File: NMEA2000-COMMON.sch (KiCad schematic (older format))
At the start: 65 parts, among them J2 CAN, SW1 PRG, SW2 INSTANCE, SW3 BUS, U1 MCP2551-I-P, U101 74LS165, U2 TMR-2-2411, U3 74HCT595, U4 74HCT595, U5 Teensy_4.0

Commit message: Tweak
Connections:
- net TRANSMIT_LED: no longer names the net of D5.2 (A), U5.17 (D15)
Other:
- moved on the sheet: C1, C3, C5, D5, F1, J2, R1, R2, R3, R36, R37, R38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

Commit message: Reroute
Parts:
- U101: value 74LS165 -> 74HC165
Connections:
- net GND: now also U101.10 (DS), U101.15 (~CE)
- net INSTANCE_CE renamed D9
- net D9: no longer U101.15 (~CE)
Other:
- note added: "CONFIGURATION"
- note removed: "Opto-isolated SPST inputs. Each opto-isolator\nis driven by a constant current source which\noperates the isolator LED at 6mA from voltages\nin the range 5VDC through 50VDC."
- moved on the sheet: C1, C101, C5, F1, J2, R1, R101, R102, R103, R104, R105, R106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

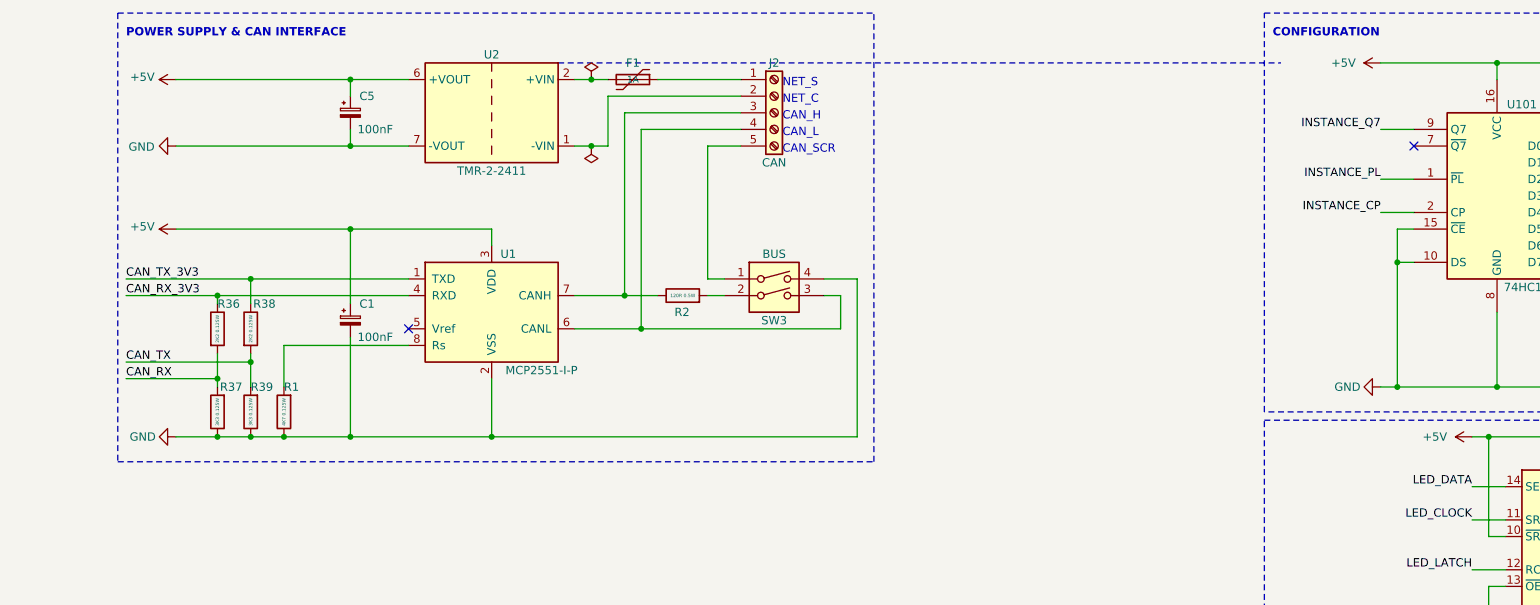
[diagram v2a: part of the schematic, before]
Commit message: Add level shifters
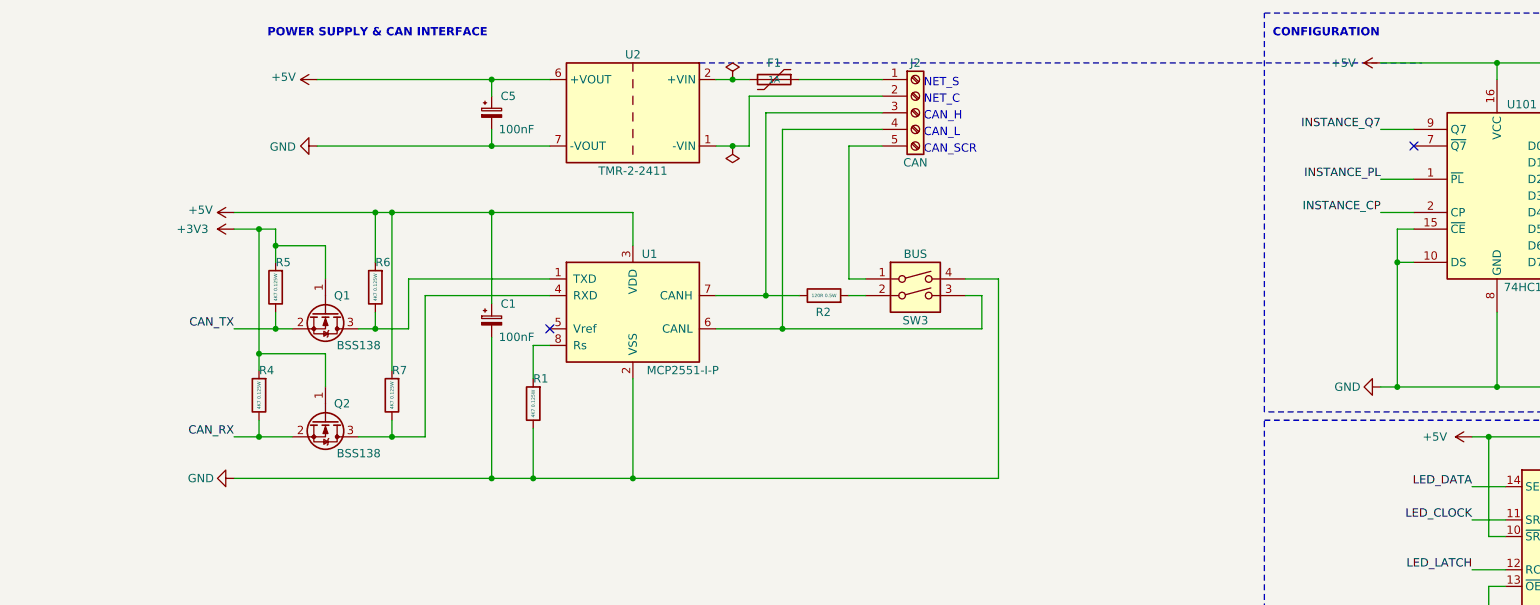
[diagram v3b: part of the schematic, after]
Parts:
- removed R36, R38: 2K2 0.125W, Resistor_SMD:R_0805_2012Metric, symbol Device:R
- removed R37, R39: 3K3 0.125W, Resistor_SMD:R_0805_2012Metric, symbol Device:R
- added Q1, Q2: BSS138, Package_TO_SOT_SMD:SOT-23, symbol Transistor_FET:BSS138
- added R4, R5, R6, R7: 4K7 0.125W, Resistor_SMD:R_0805_2012Metric, symbol Device:R
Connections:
- net +3V3: now also Q1.1 (G), Q2.1 (G), R4.2, R5.2
- net +5V: now also R6.2, R7.2
- net CAN_RX: now also Q2.2 (S), R4.1
- net CAN_TX: now also Q1.2 (S), R5.1
- net CAN_RX_3V3: no longer names the net of U1.4 (RXD)
- net CAN_RX_3V3: now also Q2.3 (D), R7.1
- net CAN_TX_3V3: no longer names the net of U1.1 (TXD)
- net CAN_TX_3V3: now also Q1.3 (D), R6.1
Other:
- moved on the sheet: C1, C5, F1, J2, R1, R2, SW3, U1, U2
